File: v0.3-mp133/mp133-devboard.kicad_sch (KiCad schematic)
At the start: 147 parts, among them CON1 microSDCon_SMT_104031-0811, J1 Pins_02x40_P0.4mm_W3.0mm_SMT, J2 Pins_02x40_P0.4mm_W3.0mm_SMT, J3 USB-C_Receptacle_Molex_217179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, J4 Pins_02x04_RightAngle_P2.54mm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, J5 Conn_01x02, J6 Pins_02x05_P1.27mm_SMT, U13 NCP51460SN33, U14 DDR3L-RAM-4Gb_MT41K256M16TW, U15 AP6230xZ6, U16 AP6230xZ6, U17 AP6230xZ6, U18 TAR5S33, U19 TAR5S33, U2 STM32MP131DAF7, U20 AP2411SN, U21 AP6230xZ6, U3 USBLC6-2SC6, U5 NORFLASH_W25Q128JV, X2 24MHz_8pF_2x1.6mm

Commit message: mp133 schematic WIP
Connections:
- net A1 is gone; now on net PA2: U2.Y4 (PA2)
- net A2 is gone; now on net PC1: U2.Y9 (PC1)
- net A3 is gone; now on net PA1: U2.AA3 (PA1)
- net A4 is gone; now on net PC4: U2.Y7 (PC4)
- net A5 is gone; now on net PB1: U2.Y8 (PB1)
- net A6 is gone; now on net PG13: U2.AA9 (PG13)
- net A7 is gone; now on net PA0: U2.Y3 (PA0)
- net A8 is gone; now on net PF11: U2.Y6 (PF11)
- net A9 is gone; now on net PB0: U2.W8 (PB0)
- net CODEC_I2C_SDA is gone; now on net PE13: U2.A3 (PE13)
- net D0 is gone; now on net PB8: U2.D1 (PB8)
- net D1 is gone; now on net PD3: U2.C2 (PD3)
- net D10 is gone; now on net PD12: U2.A6 (PD12)
- net D11 is gone; now on net PC5: U2.AA7 (PC5)
- net D12 is gone; now on net PB14: U2.B16 (PB14)
- net D16 is gone; now on net PC8: U2.C18 (PC8)
- net D17 is gone; now on net PC9: U2.A20 (PC9)
- net D18 is gone; now on net PC10: U2.A18 (PC10)
- net D19 is gone; now on net PC11: U2.B18 (PC11)
- net D2 is gone; now on net PB15: U2.B15 (PB15)
- net D3 is gone; now on net PE12: U2.A4 (PE12)
- net D4 is gone; now on net PD2: U2.C19 (PD2)
- net D5 is gone; now on net PC2: U2.AA10 (PC2)
- net D6 is gone; now on net PC3: U2.W6 (PC3)
- net D7 is gone; now on net PA6: U2.U10 (PA6)
- net D8 is gone; now on net PC0: U2.W5 (PC0)
- net D9 is gone; now on net PC12: U2.A19 (PC12)
- net SAI_MCLK is gone; now on net PA8: U2.P2 (PA8)
- net DEBUG1: now also U2.W10 (PE5)
- net DEBUG2: no longer U2.C14 (PB3)
- net DEBUG3: no longer U2.C16 (PB4)
- net DFU_BOOT: no longer U2.N1 (PE2)
- net PA10: now also U2.AA19 (PA10)
- net PA12: now also U2.F4 (PA12)
- net PA3: now also U2.W9 (PA3)
- net PA4: now also U2.AA6 (PA4)
- net PA5: now also U2.Y5 (PA5)
- net PA7: now also U2.V6 (PA7)
- net PB10: now also U2.E13 (PB10)
- net PB4: now also U2.C16 (PB4)
- net PB7: now also U2.C6 (PB7)
- net PB9: now also U2.A15 (PB9)
- net PC6: now also U2.B14 (PC6)
- net PC7: now also U2.C13 (PC7)
- net PD10: now also U2.D6 (PD10)
- net PD11: now also U2.F3 (PD11)
- net PD13: now also U2.J2 (PD13)
- net PE0: now also U2.B6 (PE0)
- net PE10: now also U2.C10 (PE10)
- net PE11: now also U2.B2 (PE11)
- net PE2: now also U2.N1 (PE2)
- net PE3: now also U2.B17 (PE3)
- net PE4: now also U2.H2 (PE4)
- net PE6: now also U2.T2 (PE6)
- net PG10: now also U2.G2 (PG10)
- net PG15: now also U2.H4 (PG15)
- net PG6: now also U2.C17 (PG6)
- net PG9: now also U2.F2 (PG9)
- net UART_RX: no longer U2.B4 (PA15)
- net UART_TX: no longer U2.A2 (PA9)
- net PF12: now reaches U2.AA4 (PF12)
- net A0 renamed PF13
- net CODEC_I2C_SCL: no longer names the net of U2.C5 (PD1)
- net CODEC_RESET: no longer names the net of U2.C1 (PB6)
- net D14: no longer names the net of U2.B7 (PE9)
- net D15: no longer names the net of U2.C4 (PD14)
- net RED_LED: no longer names the net of U2.B5 (PD8)
- net SAI_FS: no longer names the net of U2.R1 (PG1)
- net SAI_SCK: no longer names the net of U2.W2 (PG12)
- net SAI_SD_B: no longer names the net of U2.W1 (PG3)
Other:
- note added: "ADC-0"
- note added: "ADC-1"
- note added: "Add to header"
- note added: "Move to analog section on hdr"
- note added: "Remove from header"
- note removed: "ADC2_INP0"
- note removed: "ADC2_INP10"
- note removed: "SAI1_SCK_A"
- note removed: "TODO: route DFU_BOOT to some unused pin on ARM"
- moved on the sheet: C110, C111, R3, U2A, U2B, X2

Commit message: mp133 devboard sch WIP
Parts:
- removed R3: 3k_0402, 4ms_Resistor:R_0402, symbol 4ms_Resistor_0402:3k_0402
- U2: value STM32MP131DAF7 -> STM32MP133DAF
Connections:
- net USB1_DN is gone; now on net USB_HS_DM: U2.AA16 (USB_DM1)
- net USB1_DP is gone; now on net USB_HS_DP: U2.Y16 (USB_DP1)
- net DEBUG0: now also U2.C14 (PB3)
- net DEBUG1: now also U2.C16 (PB4)
- net DEBUG2: now also JP3.3 (B)
- net DEBUG3: now also JP2.1 (A)
- net PA1: now also J2.31 (Pin_31), J2.32 (Pin_32); no longer J2.39 (Pin_39), J2.40 (Pin_40)
- net PA10: no longer J1.41 (Pin_41), J1.42 (Pin_42)
- net PA11: no longer J1.61 (Pin_61), J1.62 (Pin_62)
- net PA12: no longer J1.59 (Pin_59), J1.60 (Pin_60)
- net PA2: now also J2.33 (Pin_33), J2.34 (Pin_34); no longer J2.43 (Pin_43), J2.44 (Pin_44)
- net PA3: now also J2.53 (Pin_53), J2.54 (Pin_54); no longer J2.31 (Pin_31), J2.32 (Pin_32)
- net PA4: now also J2.37 (Pin_37), J2.38 (Pin_38); no longer J2.59 (Pin_59), J2.60 (Pin_60)
- net PA5: now also J2.39 (Pin_39), J2.40 (Pin_40); no longer J2.55 (Pin_55), J2.56 (Pin_56)
- net PA7: now also J2.43 (Pin_43), J2.44 (Pin_44); no longer J2.53 (Pin_53), J2.54 (Pin_54)
- net PA8: now also J2.15 (Pin_15), J2.16 (Pin_16); no longer J1.3 (Pin_3), J1.4 (Pin_4)
- net PB0: now also J2.61 (Pin_61), J2.62 (Pin_62); no longer J2.41 (Pin_41), J2.42 (Pin_42)
- net PB1: no longer J2.45 (Pin_45), J2.46 (Pin_46)
- net PB10: no longer J1.55 (Pin_55), J1.56 (Pin_56)
- net PB7: no longer J2.10 (Pin_10), J2.9 (Pin_9)
- net PB8: no longer J2.73 (Pin_73), J2.74 (Pin_74)
- net PB9: now also J1.11 (Pin_11), J1.12 (Pin_12); no longer J1.5 (Pin_5), J1.6 (Pin_6)
- net PC0: now also J2.41 (Pin_41), J2.42 (Pin_42); no longer J2.51 (Pin_51), J2.52 (Pin_52)
- net PC1: now also J2.45 (Pin_45), J2.46 (Pin_46); no longer J2.37 (Pin_37), J2.38 (Pin_38)
- net PC2: now also J2.47 (Pin_47), J2.48 (Pin_48); no longer J2.35 (Pin_35), J2.36 (Pin_36)
- net PC3: now also J2.55 (Pin_55), J2.56 (Pin_56); no longer J2.33 (Pin_33), J2.34 (Pin_34)
- net PC5: now also J2.51 (Pin_51), J2.52 (Pin_52); no longer J2.47 (Pin_47), J2.48 (Pin_48)
- net PC6: no longer J2.13 (Pin_13), J2.14 (Pin_14)
- net PC7: no longer J1.39 (Pin_39), J1.40 (Pin_40)
- net PD10: no longer J2.3 (Pin_3), J2.4 (Pin_4)
- net PD11: no longer J1.49 (Pin_49), J1.50 (Pin_50)
- net PD12: now also J1.61 (Pin_61), J1.62 (Pin_62); no longer J1.45 (Pin_45), J1.46 (Pin_46)
- net PD13: no longer J1.47 (Pin_47), J1.48 (Pin_48)
- net PD3: no longer J1.1 (Pin_1), J1.2 (Pin_2)
- net PE0: no longer J1.43 (Pin_43), J1.44 (Pin_44)
- net PE10: no longer J1.63 (Pin_63), J1.64 (Pin_64)
- net PE11: now also J1.45 (Pin_45), J1.46 (Pin_46); no longer J2.11 (Pin_11), J2.12 (Pin_12)
- net PE12: no longer J2.19 (Pin_19), J2.20 (Pin_20)
- net PE13: no longer J2.21 (Pin_21), J2.22 (Pin_22)
- net PE2: no longer J2.69 (Pin_69), J2.70 (Pin_70)
- net PE3: no longer J2.1 (Pin_1), J2.2 (Pin_2)
- net PE4: no longer J1.11 (Pin_11), J1.12 (Pin_12)
- net PE6: no longer J2.15 (Pin_15), J2.16 (Pin_16)
- net PF11: no longer J2.61 (Pin_61), J2.62 (Pin_62)
- net PF12: now also J2.59 (Pin_59), J2.60 (Pin_60)
- net PG13: no longer J2.71 (Pin_71), J2.72 (Pin_72)
- net PG15: no longer J2.17 (Pin_17), J2.18 (Pin_18)
- net PG6: no longer J2.7 (Pin_7), J2.8 (Pin_8)
- net PG9: no longer J1.57 (Pin_57), J1.58 (Pin_58)
- net UART_RX: now also U2.B4 (PA15)
- net UART_TX: now also U2.A2 (PA9)
- net USB_RREF: now also R3.2, U2.W12 (USB_RREF)
- net PG0: now reaches U2.A7 (PG0)
- net PG4: now reaches U2.B10 (PG4)
- net PE8: now reaches U2.B9 (PE8)
- net PE8: now also J1.59 (Pin_59), J1.60 (Pin_60)
- net PG5: now reaches U2.G3 (PG5)
- net PG1: now reaches U2.R1 (PG1)
- net PG1: now also J2.21 (Pin_21), J2.22 (Pin_22)
- net PH3: now reaches U2.R3 (PH3)
- net PH3: now also J2.73 (Pin_73), J2.74 (Pin_74)
- net PG2: now reaches U2.V3 (PG2)
- net PG3: now reaches U2.W1 (PG3)
- net PG12: now reaches U2.W2 (PG12)
- net PD0: now reaches U2.B1 (PD0)
- net PD0: now also J1.43 (Pin_43), J1.44 (Pin_44)
- net PD6: now reaches U2.D2 (PD6)
- net PD6: now also J1.49 (Pin_49), J1.50 (Pin_50)
- net PD7: now reaches U2.V1 (PD7)
- net PD7: now also J2.10 (Pin_10), J2.9 (Pin_9)
- net D13 renamed PH12
- net PH12: now also J1.47 (Pin_47), J1.48 (Pin_48)
- net PB14: no longer names the net of U2.B16 (PB14)
- net PB14: no longer JP2.1 (A)
- net PB15: no longer names the net of U2.B15 (PB15)
- net PB15: no longer JP3.3 (B)
- net PB2: no longer names the net of J2.75 (Pin_75), J2.76 (Pin_76)
- net PB4: no longer names the net of J2.5 (Pin_5), J2.6 (Pin_6)
- net PB4: no longer U2.C16 (PB4)
- net SAI_SD_A renamed  PH11
- new net: J2.1 (Pin_1), J2.2 (Pin_2)
- new net: J2.13 (Pin_13), J2.14 (Pin_14)
- new net: J2.17 (Pin_17), J2.18 (Pin_18)
- new net: J2.3 (Pin_3), J2.4 (Pin_4)
- new net: J2.35 (Pin_35), J2.36 (Pin_36)
- new net: J2.69 (Pin_69), J2.70 (Pin_70)
- new net: J2.7 (Pin_7), J2.8 (Pin_8)
- new net: J2.71 (Pin_71), J2.72 (Pin_72)
- new net: J1.1 (Pin_1), J1.2 (Pin_2)
- new net: J1.3 (Pin_3), J1.4 (Pin_4)
- new net: J1.39 (Pin_39), J1.40 (Pin_40)
- new net: J1.41 (Pin_41), J1.42 (Pin_42)
- new net: J1.5 (Pin_5), J1.6 (Pin_6)
- new net: J1.55 (Pin_55), J1.56 (Pin_56)
- new net: J1.57 (Pin_57), J1.58 (Pin_58)
- new net: J1.63 (Pin_63), J1.64 (Pin_64)
- new net PH11: J2.11 (Pin_11), J2.12 (Pin_12)
- new net PH6: J2.19 (Pin_19), J2.20 (Pin_20)
- no-connect marks 46 -> 24
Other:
- note added: "ADC-6"
- note added: "ADC2-2"
- note added: "ADC2-6"
- note added: "Can swap ADC pins including these:"
- note added: "I2C-SCL(withB18)"
- note added: "I2C-SDA (with A55)"
- note added: "I2C4_SCL"
- note added: "I2C4_SDA"
- note added: "No ADC pin with MOSI and SAI_SD"
- note added: "No ADC pin with NSS and SAI_FS"
- note added: "Place these on pins:"
- note added: "Run these to a header? Jumper to sel?"
- note added: "SAI1_FS"
- note added: "SAI1_MCLK_A"
- note added: "SAI1_SCK"
- note added: "SAI2_FS_A"
- note added: "SAI2_MCLK_A"
- note added: "SAI2_SCK_A"
- note added: "SAI4_FS_A"
- note added: "SAI4_MCLK_A"
- note added: "SAI4_SD_A"
- note added: "SPI1-MISO"
- note added: "SPI1-MOSI"
- note added: "SPI1-NSS"
- note added: "SPI1-SCK"
- note added: "SPI2-MISO"
- note added: "SPI2-MOSI"
- note added: "SPI2-NSS"
- note added: "SPI2-SCK"
- note added: "TIM PWM"
- note added: "TIM15.2/2.4/5.4 PWM"
- note added: "TIM3.1/13.1"
- note added: "These probably aren't useful bec. other SAI pins don't match mp153-v0.2"
- note added: "UART_RX"
- note added: "UART_TX"
- note removed: "ADC-18"
- note removed: "ADC-18_DAC0"
- note removed: "ADC-19"
- note removed: "ADC-19_DAC1"
- note removed: "Add to header"
- note removed: "DAC0"
- note removed: "DAC1"
- note removed: "I2C2_SDA"
- note removed: "I2C5_SCL"
- note removed: "I2C5_SDA"
- note removed: "Move to analog section on hdr"
- note removed: "Remove from header"
- note removed: "SAI1_FS_A"
- note removed: "SAI4_SD_B"
- note removed: "SPI1_MISO"
- note removed: "SPI1_MOSI"
- note removed: "SPI1_NSS"
- note removed: "SPI1_SCK"
- note removed: "SPI4_MISO"
- note removed: "SPI4_MOSI"
- note removed: "SPI4_SCK"
- note removed: "UART7_RX"
- note removed: "UART7_TX"
- note removed: "USART3_RX"
- moved on the sheet: C110, C111, C12, D11, D26, R3, R76, R77, U2A, U2B, U2D, U5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

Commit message: mp133 devboard DDR routing started
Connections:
- net PB9: now also CON1.10 (SDDET1)
- net PE4: no longer CON1.10 (SDDET1)
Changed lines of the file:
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@@
 		)
 	)
+	(label "PB9"
+		(at 228.6 267.97 0)
+		(effects
+			(font
+				(size 1.27 1.27)
+			)
+			(justify left bottom)
+		)
+	)
 	(label "PC11"
 		(at 147.32 386.08 180)
@@
 		)
 	)
-	(label "PE4"
-		(at 228.6 267.97 0)
-		(effects
-			(font
-				(size 1.27 1.27)
-			)
-			(justify left bottom)
-		)
-	)
 	(label "DDR_CLK_P"
 		(at 113.03 527.05 180)
@@
 		(on_board yes)
 		(dnp no)
-		(property "Reference" "#PWR0115"
+		(property "Reference" "#PWR0101"
 			(at 341.63 396.24 0)
 			(effects
@@
 			(project "mp153-devboard"
 				(path "/64ec1a6b-f4f9-4414-abbd-a05816451f08"
-					(reference "#PWR0115")
+					(reference "#PWR0101")
 					(unit 1)
 				)

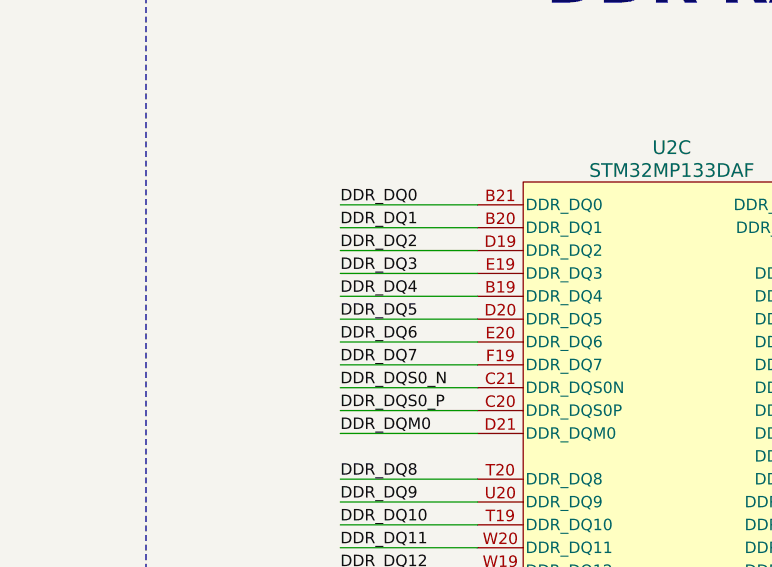
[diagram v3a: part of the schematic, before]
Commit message: mp133: add DDR pins escaped or has via
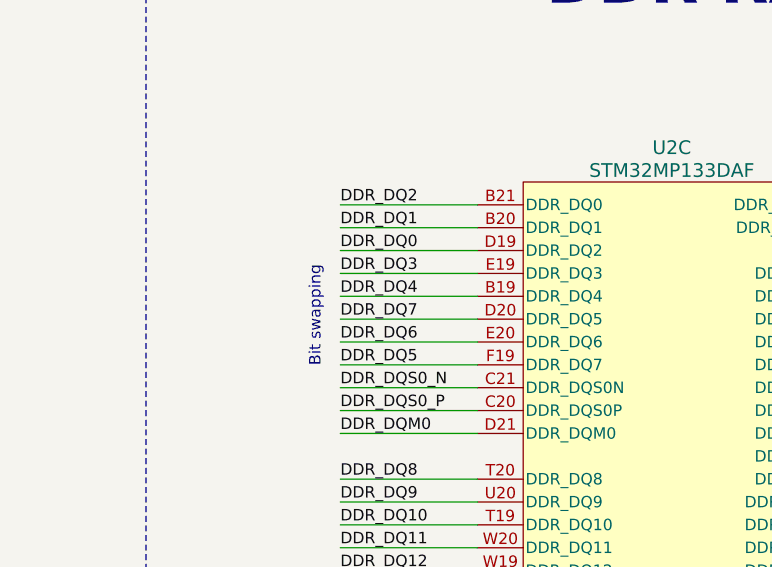
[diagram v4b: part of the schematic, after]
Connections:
- net DDR_DQ0: now also U2.D19 (DDR_DQ2); no longer U2.B21 (DDR_DQ0)
- net DDR_DQ2: now also U2.B21 (DDR_DQ0); no longer U2.D19 (DDR_DQ2)
- net DDR_DQ5: now also U2.F19 (DDR_DQ7); no longer U2.D20 (DDR_DQ5)
- net DDR_DQ7: now also U2.D20 (DDR_DQ5); no longer U2.F19 (DDR_DQ7)
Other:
- note added: "Bit swapping"
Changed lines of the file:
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@@
 		)
 	)
+	(text "Bit swapping"
+		(exclude_from_sim no)
+		(at 36.576 536.956 90)
+		(effects
+			(font
+				(size 1.27 1.27)
+			)
+		)
+	)
 	(text "SAI2_MCLK"
 		(exclude_from_sim no)
@@
 	)
 	(label "DDR_DQ5"
-		(at 39.37 537.21 0)
+		(at 39.37 542.29 0)
 		(effects
 			(font
@@
 	)
 	(label "DDR_DQ7"
-		(at 39.37 542.29 0)
+		(at 39.37 537.21 0)
 		(effects
 			(font
@@
 	)
 	(label "DDR_DQ0"
-		(at 39.37 524.51 0)
+		(at 39.37 529.59 0)
 		(effects
 			(font
@@
 	)
 	(label "DDR_DQ2"
-		(at 39.37 529.59 0)
+		(at 39.37 524.51 0)
 		(effects
 			(font

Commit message: mp13x: DDR3 RAM routed
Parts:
- U2: Manufacturer (none) -> STMicroelectronics; Part Number (none) -> STM32MP133DAF
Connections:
- net +12V is gone; now on net +5V: C14.2, U21.1 (VIN)
- net DDR_DQ0: now also U2.B21 (DDR_DQ0); no longer U2.D19 (DDR_DQ2)
- net DDR_DQ2: now also U2.D19 (DDR_DQ2); no longer U2.B21 (DDR_DQ0)
- net DDR_DQ5: now also U2.D20 (DDR_DQ5); no longer U2.F19 (DDR_DQ7)
- net DDR_DQ7: now also U2.F19 (DDR_DQ7); no longer U2.D20 (DDR_DQ5)
- net PA11: now also U2.Y1 (PA11)
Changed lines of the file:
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@@
 	(wire
 		(pts
-			(xy 43.1286 386.08) (xy 69.7986 386.08)
-		)
-		(stroke
-			(width 0)
-			(type default)
-		)
-	)
-	(wire
-		(pts
 			(xy 367.03 297.18) (xy 367.03 302.26)
 		)
@@
 	(wire
 		(pts
+			(xy 43.18 386.08) (xy 69.85 386.08)
+		)
+		(stroke
+			(width 0)
+			(type default)
+		)
+	)
+	(wire
+		(pts
 			(xy 113.03 275.59) (xy 101.6 275.59)
 		)
@@
 	)
 	(label "DDR_DQ5"
-		(at 39.37 542.29 0)
+		(at 39.37 537.21 0)
 		(effects
 			(font
@@
 	)
 	(label "DDR_DQ7"
-		(at 39.37 537.21 0)
+		(at 39.37 542.29 0)
 		(effects
 			(font
@@
 	)
 	(label "DDR_DQ0"
-		(at 39.37 529.59 0)
+		(at 39.37 524.51 0)
 		(effects
 			(font
@@
 	)
 	(label "DDR_DQ2"
-		(at 39.37 524.51 0)
+		(at 39.37 529.59 0)
 		(effects
 			(font
@@
 	)
 	(symbol
+		(lib_id "power:+5V")
+		(at 379.73 167.64 0)
+		(unit 1)
+		(exclude_from_sim no)
+		(in_bom yes)
+		(on_board yes)
+		(dnp no)
+		(fields_autoplaced yes)
+		(property "Reference" "#PWR06"
+			(at 379.73 171.45 0)
+			(effects
+				(font
+					(size 1.27 1.27)
+				)
+				(hide yes)
+			)
+		)
+		(property "Value" "+5V"
+			(at 379.73 162.56 0)
+			(effects
+				(font
+					(size 1.27 1.27)
+				)
+			)
+		)
+		(property "Footprint" ""
+			(at 379.73 167.64 0)
+			(effects
+				(font
+					(size 1.27 1.27)
+				)
+				(hide yes)
+			)
+		)
+		(property "Datasheet" ""
+			(at 379.73 167.64 0)
+			(effects
+				(font
+					(size 1.27 1.27)
+				)
+				(hide yes)
+			)
+		)
+		(property "Description" "Power symbol creates a global label with name \"+5V\""
+			(at 379.73 167.64 0)
+			(effects
+				(font
+					(size 1.27 1.27)
+				)
+				(hide yes)
+			)
+		)
+		(pin "1"
+		)
+		(instances
+			(project "mp133-devboard"
+				(path "/64ec1a6b-f4f9-4414-abbd-a05816451f08"
+					(reference "#PWR06")
+					(unit 1)
+				)
+			)
+		)
+	)
+	(symbol
 		(lib_id "4ms_Capacitor:1uF_0201_4V")
 		(at 567.69 572.77 0)
@@
 			)
 		)
-		(property "Datasheet" "STM32MP131DAF7"
+		(property "Datasheet" ""
 			(at 76.2 524.51 0)
 			(effects
@@
 			)
 		)
-		(property "Manufacturer" ""
+		(property "Manufacturer" "STMicroelectronics"
 			(at 97.79 524.51 0)
 			(effects
@@
 			)
 		)
-		(property "Part Number" ""
+		(property "Part Number" "STM32MP133DAF"
 			(at 97.79 524.51 0)
 			(effects
@@
 			)
 		)
-		(property "Datasheet" "STM32MP131DAF7"
+		(property "Datasheet" ""
 			(at 379.73 363.22 0)
 			(effects
@@
 			)
 		)
-		(property "Manufacturer" ""
+		(property "Manufacturer" "STMicroelectronics"
 			(at 401.32 363.22 0)
 			(effects
@@
 			)
 		)
-		(property "Part Number" ""
+		(property "Part Number" "STM32MP133DAF"
 			(at 401.32 363.22 0)
 			(effects
@@
 	)
 	(symbol
+		(lib_id "4ms_Power_Symbol:PWR_FLAG")
+		(at 396.24 674.37 180)
+		(unit 1)
+		(exclude_from_sim no)
+		(in_bom yes)
+		(on_board yes)
+		(dnp no)
+		(fields_autoplaced yes)
+		(property "Reference" "#FLG01"
+			(at 396.24 676.275 0)
+			(effects
+				(font
+					(size 1.27 1.27)
+				)
+				(hide yes)
+			)
+		)
+		(property "Value" "PWR_FLAG"
+			(at 396.24 678.18 0)
+			(effects
+				(font
+					(size 1.27 1.27)
+				)
+			)
+		)
+		(property "Footprint" ""
+			(at 396.24 674.37 0)
+			(effects
+				(font
+					(size 1.27 1.27)
+				)
+				(hide yes)
+			)
+		)
+		(property "Datasheet" ""
+			(at 396.24 674.37 0)
+			(effects
+				(font
+					(size 1.27 1.27)
+				)
+				(hide yes)
+			)
+		)
+		(property "Description" ""
+			(at 396.24 674.37 0)
+			(effects
+				(font
+					(size 1.27 1.27)
+				)
+				(hide yes)
+			)
+		)
+		(pin "1"
+		)
+		(instances
+			(project "mp133-devboard"
+				(path "/64ec1a6b-f4f9-4414-abbd-a05816451f08"
+					(reference "#FLG01")
+					(unit 1)
+				)
+			)
+		)
+	)
+	(symbol
 		(lib_id "power:VDD")
 		(at 519.43 463.55 0)
@@
 			)
 		)
-		(property "Datasheet" "STM32MP131DAF7"
+		(property "Datasheet" ""
 			(at 250.19 347.98 0)
 			(effects
@@
 			)
 		)
-		(property "Manufacturer" ""
+		(property "Manufacturer" "STMicroelectronics"
 			(at 228.6 347.98 0)
 			(effects
@@
 			)
 		)
-		(property "Part Number" ""
+		(property "Part Number" "STM32MP133DAF"
 			(at 228.6 347.98 0)
 			(effects
@@
 	)
 	(symbol
+		(lib_id "4ms_Power_Symbol:VDD_DDR")
+		(at 396.24 674.37 0)
+		(unit 1)
+		(exclude_from_sim no)
+		(in_bom yes)
+		(on_board yes)
+		(dnp no)
+		(fields_autoplaced yes)
+		(property "Reference" "#PWR043"
+			(at 396.24 674.37 0)
+			(effects
+				(font
+					(size 1.27 1.27)
+				)
+				(hide yes)
+			)
+		)
+		(property "Value" "VDD_DDR"
+			(at 396.24 670.814 0)
+			(effects
+				(font
+					(size 1.27 1.27)
+				)
+			)
+		)
+		(property "Footprint" ""
+			(at 396.24 674.37 0)
+			(effects
+				(font
+					(size 1.27 1.27)
+				)
+				(hide yes)
+			)
+		)
+		(property "Datasheet" ""
+			(at 396.24 674.37 0)
+			(effects
+				(font
+					(size 1.27 1.27)
+				)
+				(hide yes)
+			)
+		)
+		(property "Description" ""
+			(at 396.24 674.37 0)
+			(effects
+				(font
+					(size 1.27 1.27)
+				)
+				(hide yes)
+			)
+		)
+		(pin "1"
+		)
+		(instances
+			(project "mp133-devboard"
+				(path "/64ec1a6b-f4f9-4414-abbd-a05816451f08"
+					(reference "#PWR043")
+					(unit 1)
+				)
+			)
+		)
+	)
+	(symbol
 		(lib_id "4ms_Power_Symbol:GND")
 		(at 566.42 596.9 0)
@@
 			)
 		)
-		(property "Datasheet" "STM32MP131DAF7"
+		(property "Datasheet" ""
 			(at 549.91 288.29 0)
 			(effects
@@
 			)
 		)
-		(property "Manufacturer" ""
+		(property "Manufacturer" "STMicroelectronics"
 			(at 571.5 288.29 0)
 			(effects
@@
 			)
 		)
-		(property "Part Number" ""
+		(property "Part Number" "STM32MP133DAF"
 			(at 571.5 288.29 0)
 			(effects
@@
 	)
 	(symbol
-		(lib_id "4ms_Power_Symbol:+12V")
-		(at 379.73 167.64 0)
-		(unit 1)
-		(exclude_from_sim no)
-		(in_bom yes)
-		(on_board yes)
-		(dnp no)
-		(fields_autoplaced yes)
-		(property "Reference" "#PWR0200"
-			(at 379.73 171.45 0)
-			(effects
-				(font
-					(size 1.27 1.27)
-				)
-				(hide yes)
-			)
-		)
-		(property "Value" "+12V"
-			(at 379.73 164.084 0)
-			(effects
-				(font
-					(size 1.27 1.27)
-				)
-			)
-		)
-		(property "Footprint" ""
-			(at 379.73 167.64 0)
-			(effects
-				(font
-					(size 1.27 1.27)
-				)
-				(hide yes)
-			)
-		)
-		(property "Datasheet" ""
-			(at 379.73 167.64 0)
-			(effects
-				(font
-					(size 1.27 1.27)
-				)
-				(hide yes)
-			)
-		)
-		(property "Description" ""
-			(at 379.73 167.64 0)
-			(effects
-				(font
-					(size 1.27 1.27)
-				)
-			)
-		)
-		(pin "1"
-		)
-		(instances
-			(project "mp153-devboard"
-				(path "/64ec1a6b-f4f9-4414-abbd-a05816451f08"
-					(reference "#PWR0200")
-					(unit 1)
-				)
-			)
-		)
-	)
-	(symbol
 		(lib_id "4ms_Power_Symbol:GND")
 		(at 191.77 668.02 0)
@@
 			)
 		)
-		(property "Datasheet" "STM32MP131DAF7"
+		(property "Datasheet" ""
 			(at 91.44 358.14 0)
 			(effects
@@
 			)
 		)
-		(property "Manufacturer" ""
+		(property "Manufacturer" "STMicroelectronics"
 			(at 69.85 358.14 0)
 			(effects
@@
 			)
 		)
-		(property "Part Number" ""
+		(property "Part Number" "STM32MP133DAF"
 			(at 69.85 358.14 0)
 			(effects
